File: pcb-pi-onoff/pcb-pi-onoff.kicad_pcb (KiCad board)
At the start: 2 copper layers, 65 x 30 mm, 31 parts, among them J1 Conn_02x20_Odd_Even, J3 Conn_01x06_Male, J4 USB_B_Micro, J5 RUN/~PGM~, J6 Conn_01x03_Male, J7 Conn_SW1, J8 Conn_01x02_Bat, Q1 AO3401A, SW1 SW_Push, U1 TSOP4838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

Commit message: added url/revision on B.SilkS
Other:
- board text added: "https://github.com/bablokb/pcb-pi-onoff Rev: 1.0"

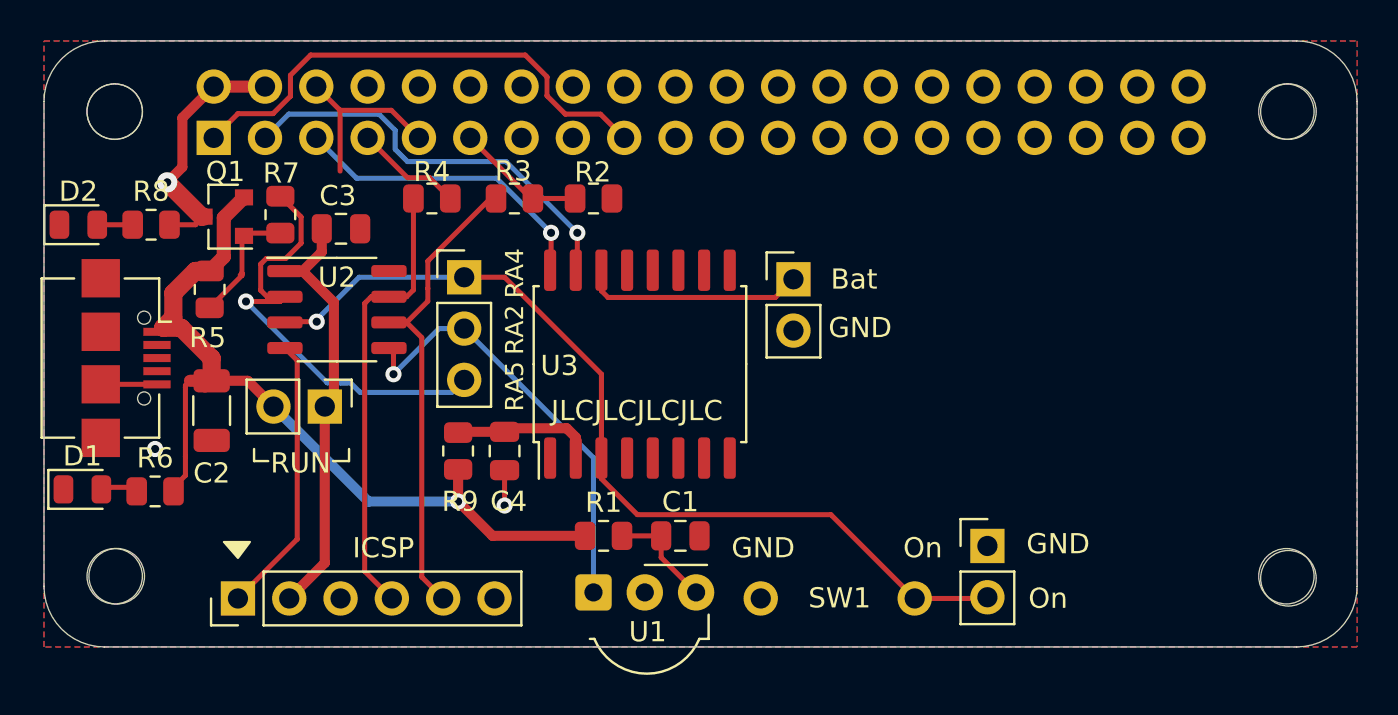
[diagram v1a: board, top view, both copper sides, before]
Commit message: added I2C-connector
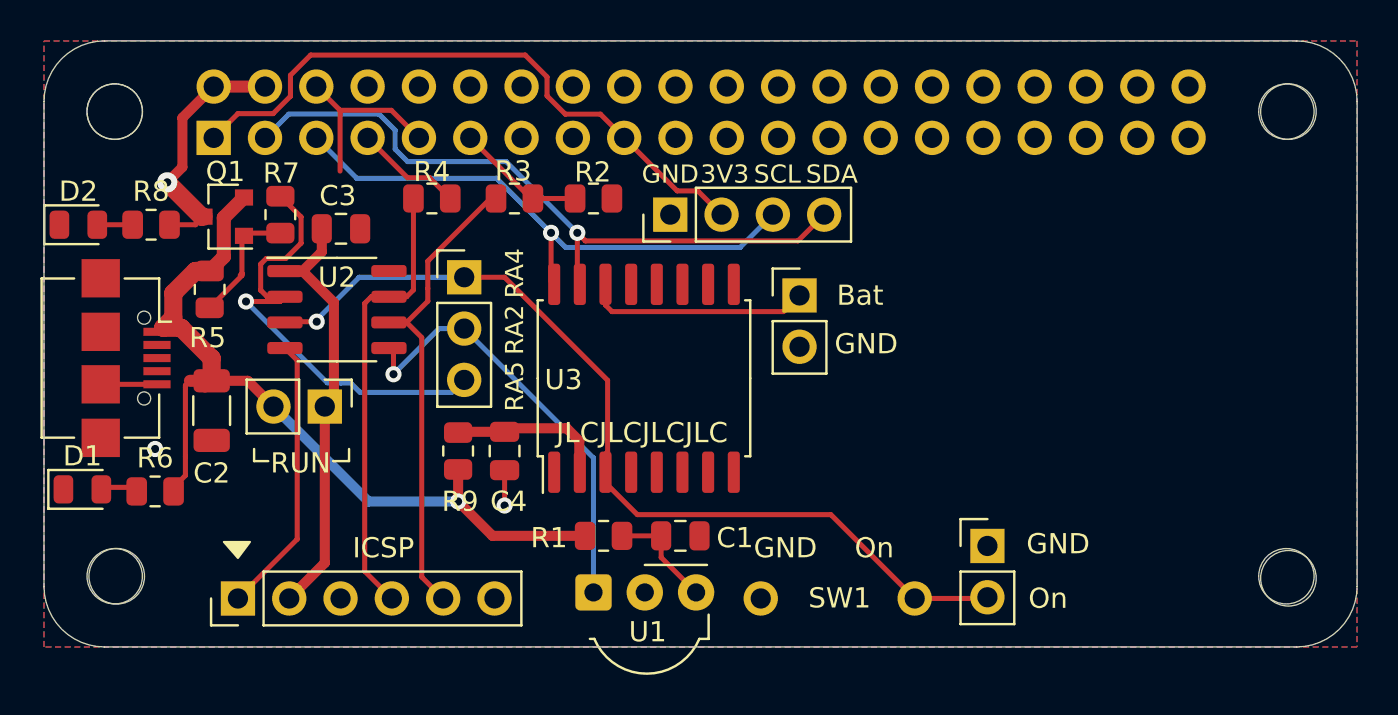
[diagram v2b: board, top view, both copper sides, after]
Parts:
- added J2: Conn_01x04_I2C, Connector_PinHeader_2.54mm:PinHeader_1x04_P2.54mm_Vertical, F.Cu at (81.0, 57.6)
- moved J8 0.85 mm to (87.4, 61.6)
- moved U3 0.73 mm to (79.7, 65.7)
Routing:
- net /GPIO2(SDA1): track 20.8 -> 34.5 mm
- net /GPIO3(SCL1): track 15.4 -> 28.1 mm
- net +3V3: track 24.9 -> 31.3 mm
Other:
- board text added: "3V3"
- board text added: "SCL"
- board text added: "SDA"

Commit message: added SPI-connector
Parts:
- added J9: Conn_01x06_SPI, Connector_PinHeader_2.54mm:PinHeader_1x06_P2.54mm_Vertical, F.Cu at (105.1, 57.6)
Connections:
- J1 pad 19: Net-(J1-Pad19) -> /GPIO10(SPI-TX)
- J1 pad 21: Net-(J1-Pad21) -> /GPIO9(SPI-RX)
- J1 pad 23: Net-(J1-Pad23) -> /GPIO11(SPI-CLK)
- J1 pad 24: Net-(J1-Pad24) -> /GPIO8(SPI-CE0)
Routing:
- net /GPIO9(SPI-RX): track 0.00 -> 25.1 mm
- net /GPIO10(SPI-TX): track 0.00 -> 22.0 mm
- net /GPIO8(SPI-CE0): track 0.00 -> 19.9 mm
- net /GPIO11(SPI-CLK): track 0.00 -> 12.7 mm
- net +3V3: track 31.3 -> 41.1 mm
- net GND: track 13.7 -> 20.9 mm
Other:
- board text added: "CE0"
- board text added: "CLK"
- board text added: "RX"
- board text added: "TX"

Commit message: added GPIO-connector
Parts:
- added J10: Conn_02x06_GPIO, Connector_PinHeader_2.54mm:PinHeader_2x06_P2.54mm_Vertical, F.Cu at (112.7, 70.2)
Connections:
- J1 pad 29: Net-(J1-Pad29) -> /GPIO5
- J1 pad 31: Net-(J1-Pad31) -> /GPIO6
- J1 pad 33: Net-(J1-Pad33) -> /GPIO13
- J1 pad 35: Net-(J1-Pad35) -> /GPIO19
- J1 pad 36: Net-(J1-Pad36) -> /GPIO16
- J1 pad 37: Net-(J1-Pad37) -> /GPIO26
- J1 pad 38: Net-(J1-Pad38) -> /GPIO20
- J1 pad 40: Net-(J1-Pad40) -> /GPIO21
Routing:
- net /GPIO16: track 0.00 -> 26.7 mm
- net +3V3: track 41.1 -> 66.6 mm
- net /GPIO5: track 0.00 -> 23.1 mm
- net /GPIO6: track 0.00 -> 19.5 mm
- net /GPIO26: track 0.00 -> 17.4 mm
- net /GPIO13: track 0.00 -> 15.9 mm
- net /GPIO20: track 0.00 -> 15.5 mm
- net /GPIO19: track 0.00 -> 12.7 mm
- net /GPIO21: track 0.00 -> 11.3 mm
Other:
- board text added: "GND 19 13 06 05 3V3"
- board text added: "GND 21 20 26 16 3V3"

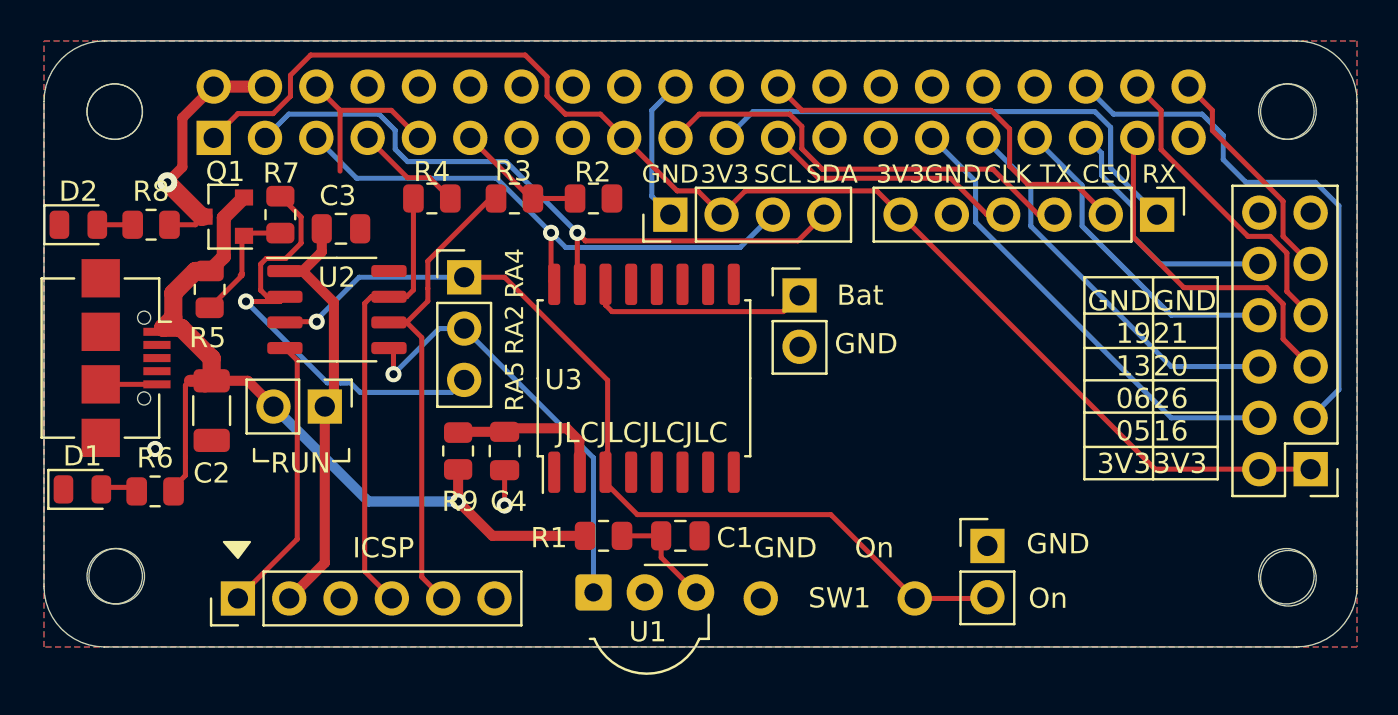
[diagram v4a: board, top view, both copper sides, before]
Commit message: replaced footprints for PIC and RTC with handsolder-version
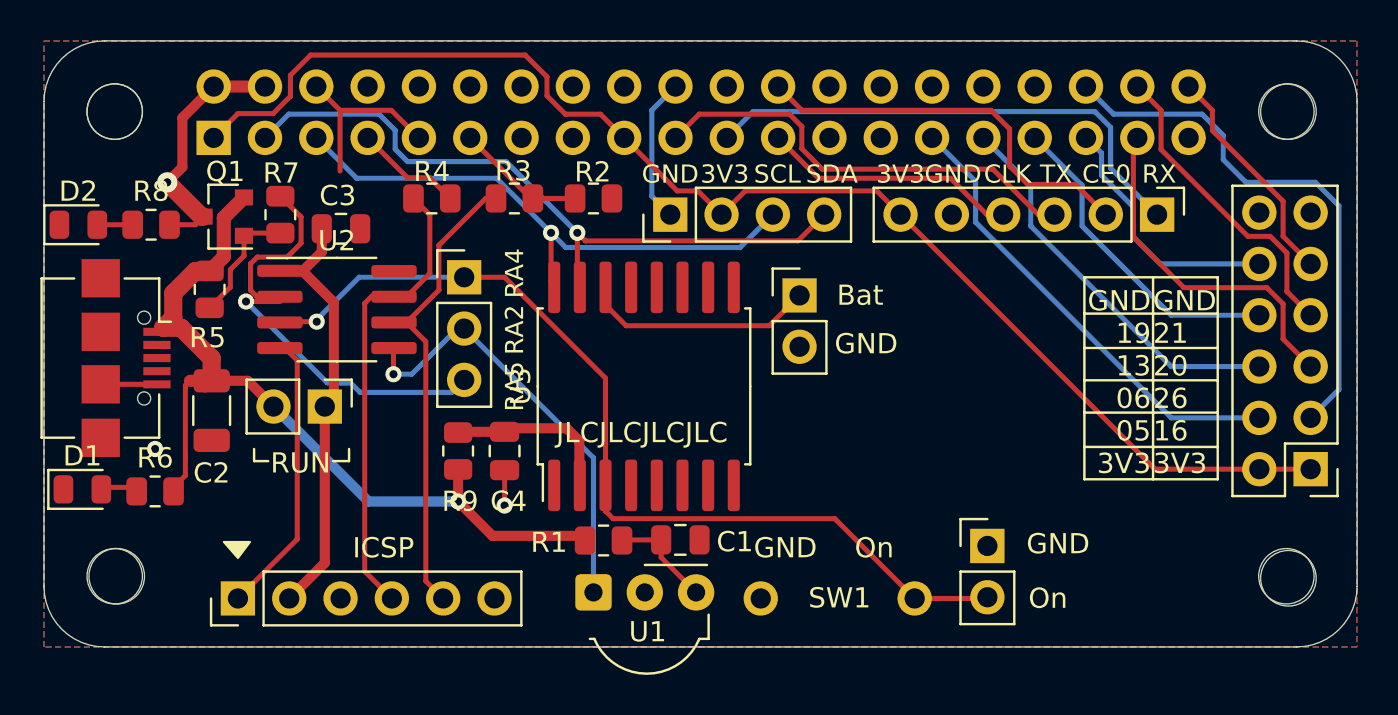
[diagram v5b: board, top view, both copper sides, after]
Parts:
- U2: footprint Package_SO:SO-8_3.9x4.9mm_P1.27mm -> user:SO-8_3.9x4.9mm_P1.27mm_HandSolder
- U3: footprint Package_SO:SOIC-16W_7.5x10.3mm_P1.27mm -> user:SOIC-16W_7.5x10.3mm_P1.27mm_HandSolder
- moved U3 0.40 mm to (79.7, 66.1)
- moved R1 0.23 mm to (77.7, 73.7)
- moved C1 0.20 mm to (81.5, 73.7)
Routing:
- net /VCC: track 7.02 -> 8.56 mm
- net /~INT: track 45.5 -> 46.7 mm
- net /DAT: track 22.4 -> 23.1 mm
- net /VBAT: track 11.1 -> 11.7 mm

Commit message: Rev 1.0: changed 3V3/GND on GPIO-connector
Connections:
- J10 pad 1: +3V3 -> GND
- J10 pad 12: GND -> +3V3
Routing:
- net GND: track 20.9 -> 45.3 mm
- net +3V3: track 66.6 -> 77.8 mm
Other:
- board text added: "3V3 19 13 06 05 3V3"
- board text added: "GND 21 20 26 16 GND"
- board text removed: "GND 19 13 06 05 3V3"
- board text removed: "GND 21 20 26 16 3V3"
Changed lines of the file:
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@@
   (general
     (thickness 1.6)
-    (drawings 83)
-    (tracks 255)
+    (drawings 81)
+    (tracks 266)
     (zones 0)
     (modules 34)
@@
     (pad_to_mask_clearance 0)
     (aux_axis_origin 0 0)
-    (visible_elements 7FFFFFFF)
+    (visible_elements 7FFFEFFF)
     (pcbplotparams
       (layerselection 0x010f0_ffffffff)
@@
     (tags "SOIC SO")
     (attr smd)
-    (fp_text reference U3 (at 0 -6.1 90) (layer F.SilkS)
+    (fp_text reference U3 (at 0.6 -4.4 90) (layer F.SilkS)
       (effects (font (size 1 1) (thickness 0.15)))
     )
     (fp_text value DS3231M (at 0 6.1 90) (layer F.Fab)
-      (effects (font (size 1 1) (thickness 0.15)))
-    )
-    (fp_text user %R (at 0 0 90) (layer F.Fab)
       (effects (font (size 1 1) (thickness 0.15)))
     )
@@
     (fp_line (start 6.43 5.4) (end 6.43 -5.4) (layer F.CrtYd) (width 0.05))
     (fp_line (start 6.43 -5.4) (end -6.43 -5.4) (layer F.CrtYd) (width 0.05))
+    (fp_text user %R (at 0 0 90) (layer F.Fab)
+      (effects (font (size 1 1) (thickness 0.15)))
+    )
     (pad 16 smd roundrect (at 4.9 -4.445 90) (size 2.55 0.6) (layers F.Cu F.Paste F.Mask) (roundrect_rratio 0.25)
       (net 3 "/GPIO3(SCL1)"))
@@
     (fp_text value PIC12F1840 (at 0 3.4) (layer F.Fab)
       (effects (font (size 1 1) (thickness 0.15)))
-    )
-    (fp_text user %R (at 0 0) (layer F.Fab)
-      (effects (font (size 0.98 0.98) (thickness 0.15)))
     )
     (fp_line (start 0 2.56) (end 1.95 2.56) (layer F.SilkS) (width 0.12))
@@
     (fp_line (start 4.2 2.7) (end 4.2 -2.7) (layer F.CrtYd) (width 0.05))
     (fp_line (start 4.2 -2.7) (end -4.2 -2.7) (layer F.CrtYd) (width 0.05))
+    (fp_text user %R (at 0 0) (layer F.Fab)
+      (effects (font (size 0.98 0.98) (thickness 0.15)))
+    )
     (pad 8 smd roundrect (at 2.825 -1.905) (size 2.25 0.6) (layers F.Cu F.Paste F.Mask) (roundrect_rratio 0.25)
       (net 1 GND))
@@
     )
     (pad 12 thru_hole oval (at 2.54 12.7 180) (size 1.7 1.7) (drill 1) (layers *.Cu *.Mask)
-      (net 1 GND))
+      (net 2 +3V3))
     (pad 11 thru_hole oval (at 0 12.7 180) (size 1.7 1.7) (drill 1) (layers *.Cu *.Mask)
       (net 1 GND))
@@
       (net 2 +3V3))
     (pad 1 thru_hole rect (at 0 0 180) (size 1.7 1.7) (drill 1) (layers *.Cu *.Mask)
-      (net 2 +3V3))
+      (net 1 GND))
     (model ${KISYS3DMOD}/Connector_PinHeader_2.54mm.3dshapes/PinHeader_2x06_P2.54mm_Vertical.wrl
       (at (xyz 0 0 0))
@@
   (gr_line (start 108.1 60.7) (end 108.1 70.7) (layer F.SilkS) (width 0.12))
   (gr_line (start 101.5 60.7) (end 108.1 60.7) (layer F.SilkS) (width 0.12))
-  (gr_text "GND\n21\n20\n26\n16\n3V3" (at 104.9 65.9) (layer F.SilkS)
+  (gr_text "GND\n21\n20\n26\n16\nGND" (at 104.9 65.9) (layer F.SilkS)
     (effects (font (size 1 1) (thickness 0.15)) (justify left))
   )
-  (gr_text "GND\n19\n13\n06\n05\n3V3" (at 104.8 65.9) (layer F.SilkS)
+  (gr_text "3V3\n19\n13\n06\n05\n3V3" (at 104.8 65.9) (layer F.SilkS)
     (effects (font (size 1 1) (thickness 0.15)) (justify right))
   )
@@
   )
   (gr_text Bat (at 90.4 61.6) (layer F.SilkS)
-    (effects (font (size 1 1) (thickness 0.15)))
-  )
-  (gr_text GND (at 86.7 74.1) (layer F.SilkS)
-    (effects (font (size 1 1) (thickness 0.15)))
-  )
-  (gr_text On (at 91.1 74.1) (layer F.SilkS)
     (effects (font (size 1 1) (thickness 0.15)))
   )
@@
   (segment (start 80.084999 52.435001) (end 80.084999 56.684999) (width 0.25) (layer B.Cu) (net 1))
   (segment (start 81.26 51.26) (end 80.084999 52.435001) (width 0.25) (layer B.Cu) (net 1))
+  (segment (start 114 68.9) (end 112.7 70.2) (width 0.25) (layer F.Cu) (net 1))
+  (segment (start 114 58.8) (end 114 68.9) (width 0.25) (layer F.Cu) (net 1))
+  (segment (start 112.7 57.5) (end 114 58.8) (width 0.25) (layer F.Cu) (net 1))
+  (segment (start 104.684001 50.084999) (end 100.215001 50.084999) (width 0.25) (layer F.Cu) (net 1))
+  (segment (start 100.215001 50.084999) (end 99.04 51.26) (width 0.25) (layer F.Cu) (net 1))
+  (segment (start 105.295001 50.695999) (end 104.684001 50.084999) (width 0.25) (layer F.Cu) (net 1))
+  (segment (start 105.295001 51.634003) (end 105.295001 50.695999) (width 0.25) (layer F.Cu) (net 1))
+  (segment (start 106.66 52.999002) (end 105.295001 51.634003) (width 0.25) (layer F.Cu) (net 1))
+  (segment (start 106.66 53.8) (end 106.66 52.999002) (width 0.25) (layer F.Cu) (net 1))
   (segment (start 59.6 52.6) (end 58.4 53.8) (width 0.25) (layer F.Cu) (net 2))
   (segment (start 62.2 50.7) (end 62.2 51.739002) (width 0.25) (layer F.Cu) (net 2))
@@
   (segment (start 105 70.2) (end 110.16 70.2) (width 0.25) (layer F.Cu) (net 2))
   (segment (start 92.4 57.6) (end 105 70.2) (width 0.25) (layer F.Cu) (net 2))
-  (segment (start 110.16 70.2) (end 112.7 70.2) (width 0.25) (layer F.Cu) (net 2))
+  (segment (start 111.335001 58.675001) (end 110.16 57.5) (width 0.25) (layer B.Cu) (net 2))
+  (segment (start 111.335001 69.024999) (end 111.335001 58.675001) (width 0.25) (layer B.Cu) (net 2))
+  (segment (start 110.16 70.2) (end 111.335001 69.024999) (width 0.25) (layer B.Cu) (net 2))
   (segment (start 63.48 53.8) (end 65.48 55.8) (width 0.25) (layer B.Cu) (net 3))
   (via (at 75.1 58.5) (size 0.8) (drill 0.4) (layers F.Cu B.Cu) (net 3))
